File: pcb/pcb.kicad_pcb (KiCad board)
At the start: 2 copper layers, 176 x 59.6 mm, 39 parts, among them J1 Conn_01x04, J2 Conn_01x04, J3 UPDI, SW1 MX Grey w/ LED, SW2 MX Grey w/ LED, SW3 1241.1100.7095, U1 Display Driver, U2 Display Driver, U3 MCU, U4 OR, 2 Channels, U5 Voltage Regulator, Y1 32kHz

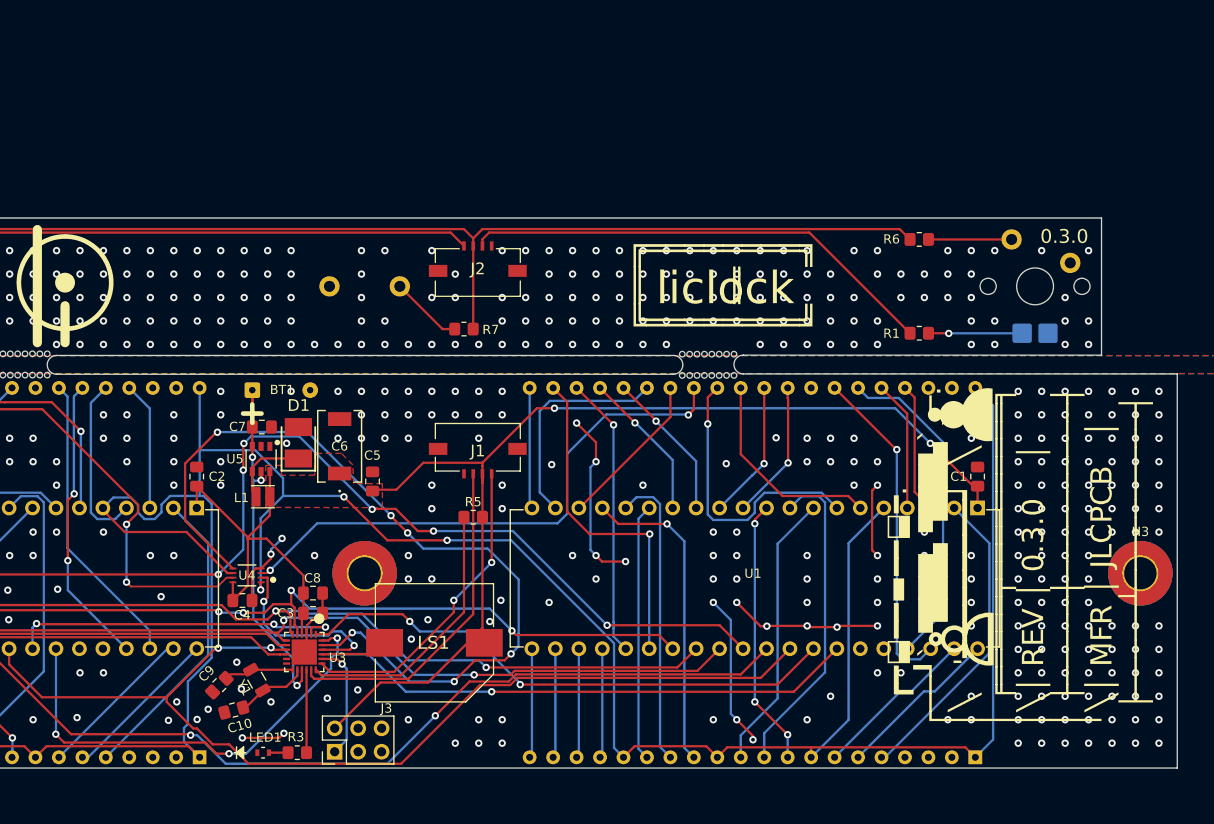
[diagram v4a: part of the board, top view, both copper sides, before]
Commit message: Fix mounting hole margin
Signed-off-by: Michael Darr <mdarr@tesla.com>
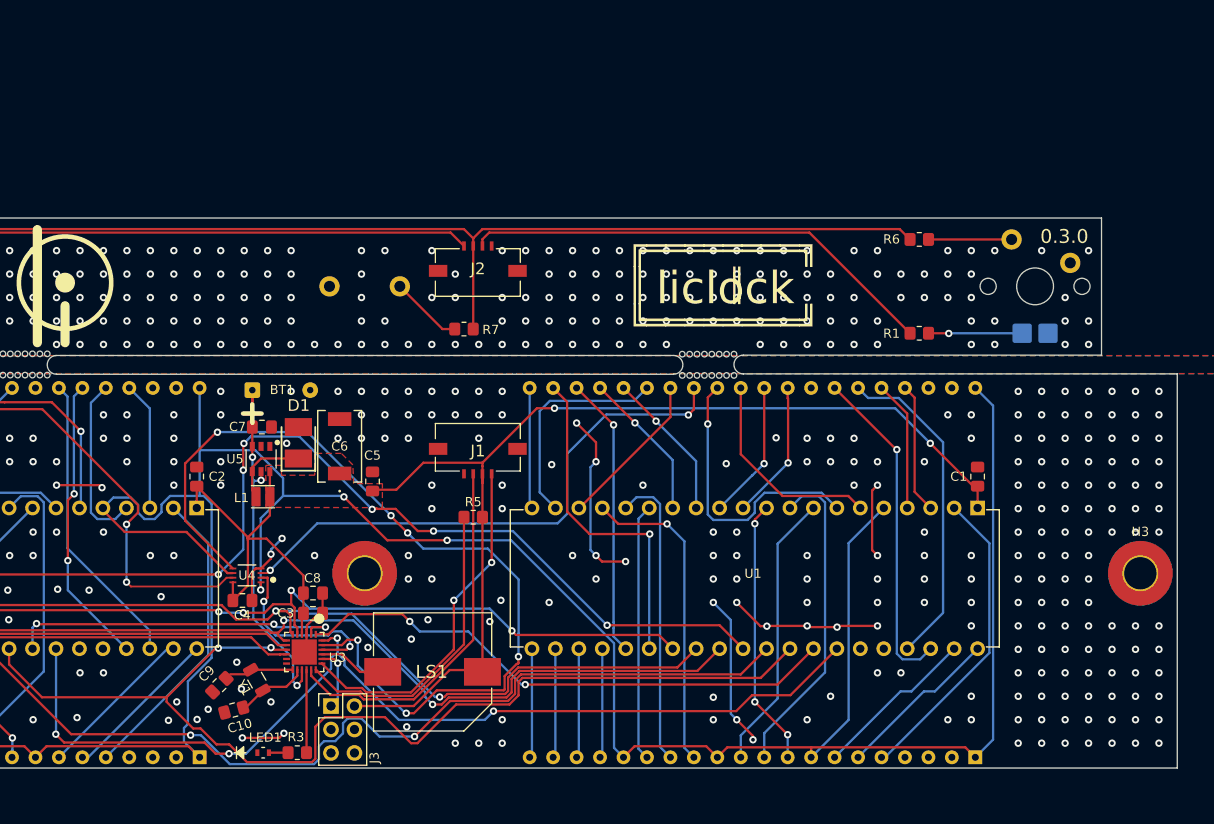
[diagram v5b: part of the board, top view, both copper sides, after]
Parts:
- moved J3 4.97 mm to (145.8, 129.9), turned to 0 degrees
- moved LS1 3.16 mm to (156.8, 126.2)
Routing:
- net UPDI: track 12.7 -> 6.79 mm
- net COL_1: track 90.6 -> 96.3 mm
- net DIGIT2: track 111.5 -> 116.6 mm
- net GND: track 80.7 -> 85.7 mm, vias 430 -> 431
- net /SW2_LED: track 34.2 -> 38.4 mm
- net DIGIT1: track 128.7 -> 132.7 mm
- net /SW_READ: track 29.8 -> 33.6 mm
- net DATA2: track 91.7 -> 95.3 mm
- net DATA1: track 104.1 -> 107.6 mm
- net /SW1_LED: track 36.4 -> 39.9 mm
- net LCD_WRITE: track 107.0 -> 109.8 mm
- net COL_2: track 20.7 -> 20.2 mm
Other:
- board text removed: "┏━⬓━━▬━━⬓━. ┌──┚`▝███▖▜██▙`ˎ─. │╲ ꞌ━━━━━━━━━┙ ╲ │ ╒═════╤══════════╕ │╲│ REV │ 0.3.0 │ │ ├─────┼──────────┤ ╵╲│ MFR │ JLCPCB │ ├─────┴──────────┤"
- board text removed: "♙"
- board text removed: "♟"

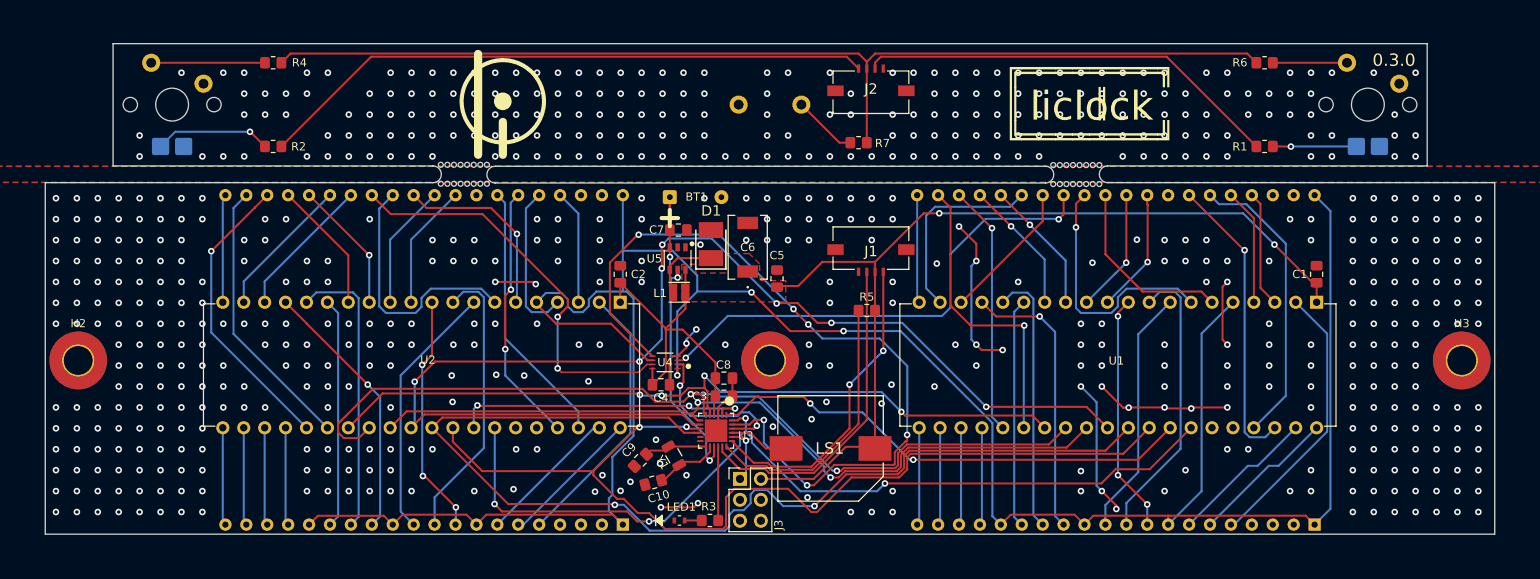
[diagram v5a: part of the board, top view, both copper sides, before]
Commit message: Add extensive mounting holes
Signed-off-by: Michael Darr <mdarr@tesla.com>
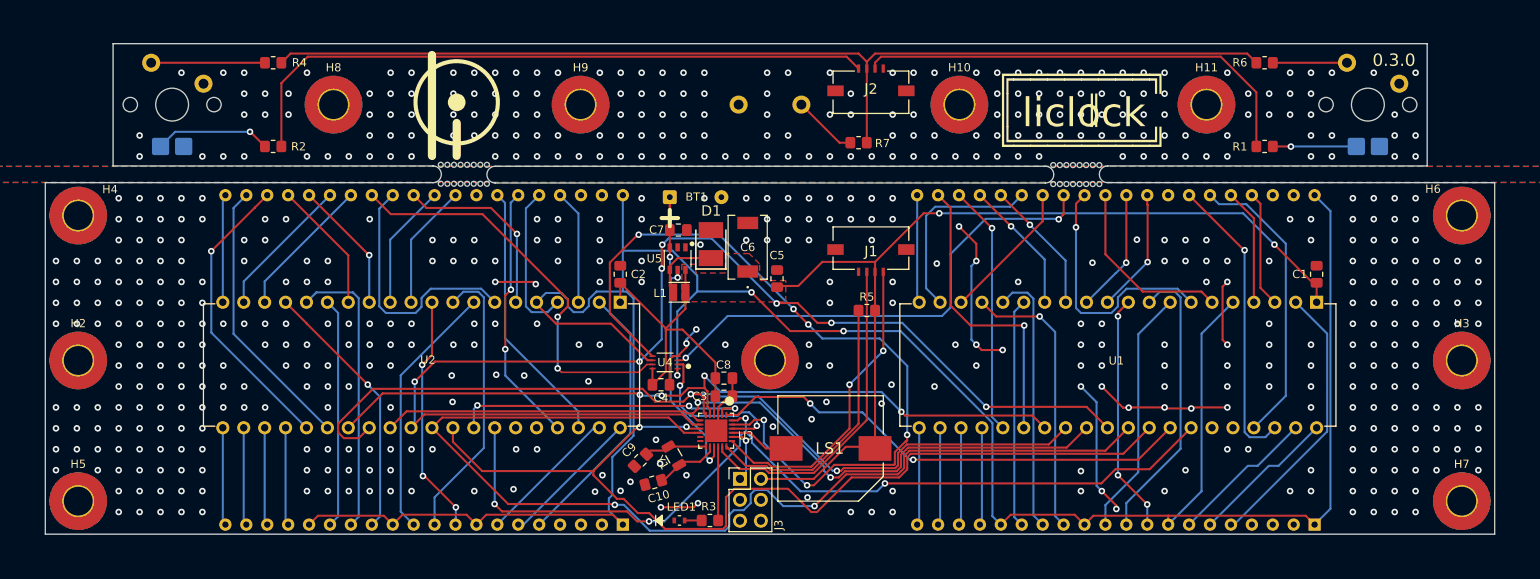
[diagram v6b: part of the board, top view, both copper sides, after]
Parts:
- added H10: MountingHole_Pad, MountingHole:MountingHole_3.5mm_Pad_TopBottom, F.Cu at (172.4, 84.5)
- added H11: MountingHole_Pad, MountingHole:MountingHole_3.5mm_Pad_TopBottom, F.Cu at (202.4, 84.5)
- added H4: MountingHole_Pad, MountingHole:MountingHole_3.5mm_Pad_TopBottom, F.Cu at (65.4, 98.0)
- added H5: MountingHole_Pad, MountingHole:MountingHole_3.5mm_Pad_TopBottom, F.Cu at (65.4, 132.7)
- added H6: MountingHole_Pad, MountingHole:MountingHole_3.5mm_Pad_TopBottom, F.Cu at (233.4, 98.0)
- added H7: MountingHole_Pad, MountingHole:MountingHole_3.5mm_Pad_TopBottom, F.Cu at (233.4, 132.7)
- added H8: MountingHole_Pad, MountingHole:MountingHole_3.5mm_Pad_TopBottom, F.Cu at (96.4, 84.5)
- added H9: MountingHole_Pad, MountingHole:MountingHole_3.5mm_Pad_TopBottom, F.Cu at (126.4, 84.5)
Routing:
- net Net-(J2-Pad1): track 75.2 -> 79.7 mm
- net Net-(J2-Pad3): track 51.8 -> 55.7 mm
- net GND1: vias 222 -> 195
- net GND: vias 431 -> 399
